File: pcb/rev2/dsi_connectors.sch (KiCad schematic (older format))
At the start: 6 parts, among them CN2 AX3E41264, CN3 CONN_02X15_ALT

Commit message: pcb wip
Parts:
- added B5, B6: PLATED_HOLE0.8_PAD1.3, c130h80, symbol PLATED_HOLE0.8_PAD1.3
- CN2: footprint (none) -> dsi_shield:IPHONE4_LCD_CONN
- CN3: footprint (none) -> dsi_shield:GB042-30S-E1000
- R1, R2, R49, R50: footprint RESC1608X55N -> Resistors SMD:RESC1608X55N
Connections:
- net labels added: +5V
- wire segments 79 -> 83
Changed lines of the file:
@@
 F 0 "CN2" H 6450 2865 50  0000 C CNN
 F 1 "AX3E41264" H 6450 2774 50  0000 C CNN
-F 2 "" H 6450 900 50  0001 C CNN
+F 2 "dsi_shield:IPHONE4_LCD_CONN" H 6450 900 50  0001 C CNN
 F 3 "" H 6450 900 50  0001 C CNN
 	1    6450 2050
@@
 F 0 "R1" H 7650 1853 50  0000 C CNN
 F 1 "R0603_10R_1%_0.1W_200PPM" H 7500 1340 60  0001 L CNN
-F 2 "RESC1608X55N" H 7500 530 60  0001 L CNN
+F 2 "Resistors SMD:RESC1608X55N" H 7500 530 60  0001 L CNN
 F 3 "\\cern.ch\\dfs\\Applications\\Altium\\Datasheets\\R0603_NIC_NRC.pdf" H 7500 1160 60  0001 L CNN
 F 4 "Value" H 7500 1550 60  0001 C CNN "Fieldname"
@@
 F 0 "R2" H 7650 2147 50  0000 C CNN
 F 1 "R0603_3K3_1%_0.1W_100PPM" H 7500 1740 60  0001 L CNN
-F 2 "RESC1608X55N" H 7500 930 60  0001 L CNN
+F 2 "Resistors SMD:RESC1608X55N" H 7500 930 60  0001 L CNN
 F 3 "\\cern.ch\\dfs\\Applications\\Altium\\Datasheets\\R0603_NIC_NRC.pdf" H 7500 1560 60  0001 L CNN
 F 4 "3k3" H 7650 2056 50  0000 C CNN "~"
@@
 F 0 "CN3" H 6450 5865 50  0000 C CNN
 F 1 "CONN_02X15_ALT" H 6450 5774 50  0000 C CNN
-F 2 "" H 6450 3800 50  0001 C CNN
+F 2 "dsi_shield:GB042-30S-E1000" H 6450 3800 50  0001 C CNN
 F 3 "" H 6450 3800 50  0001 C CNN
 	1    6450 4950
@@
 F 0 "R49" H 7300 4547 50  0000 C CNN
 F 1 "R0603_10R_1%_0.1W_200PPM" H 7150 4140 60  0001 L CNN
-F 2 "RESC1608X55N" H 7150 3330 60  0001 L CNN
+F 2 "Resistors SMD:RESC1608X55N" H 7150 3330 60  0001 L CNN
 F 3 "\\cern.ch\\dfs\\Applications\\Altium\\Datasheets\\R0603_NIC_NRC.pdf" H 7150 3960 60  0001 L CNN
 F 4 "10" H 7300 4456 50  0000 C CNN "~"
@@
 F 0 "R50" H 7300 4345 50  0000 C CNN
 F 1 "R0603_10R_1%_0.1W_200PPM" H 7150 4240 60  0001 L CNN
-F 2 "RESC1608X55N" H 7150 3430 60  0001 L CNN
+F 2 "Resistors SMD:RESC1608X55N" H 7150 3430 60  0001 L CNN
 F 3 "\\cern.ch\\dfs\\Applications\\Altium\\Datasheets\\R0603_NIC_NRC.pdf" H 7150 4060 60  0001 L CNN
 F 4 "10" H 7450 4350 50  0000 C CNN "~"
@@
 Wire Notes Line
 	3100 6800 700  6800
+$Comp
+L PLATED_HOLE0.8_PAD1.3 B5
+U 1 1 599E1A70
+P 2500 5000
+F 0 "B5" H 2485 5105 50  0000 C CNN
+F 1 "PLATED_HOLE0.8_PAD1.3" H 2500 4830 60  0001 L CNN
+F 2 "c130h80" H 2500 4020 60  0001 L CNN
+F 3 "Undefined" H 2500 4650 60  0001 L CNN
+F 4 "Plated Hole" H 2500 4560 60  0001 L CNN "Field4"
+F 5 "PLATED_HOLE0.8_PAD1.3" H 2500 4560 60  0001 L CNN "Part Number"
+F 6 "Single Terminal Socket" H 2500 4470 60  0001 L CNN "Library Ref"
+F 7 "SchLib\\Pads.SchLib" H 2500 4380 60  0001 L CNN "Library Path"
+F 8 "~~" H 2500 4290 60  0001 L CNN "Comment"
+F 9 "Standard (No BOM)" H 2500 4200 60  0001 L CNN "Component Kind"
+F 10 "Standard (No BOM)" H 2500 4110 60  0001 L CNN "Component Type"
+F 11 "1" H 2500 3930 60  0001 L CNN "Pin Count"
+F 12 "~~" H 2500 3840 60  0001 L CNN "Case"
+F 13 "PcbLib\\Pads.PcbLib" H 2500 3750 60  0001 L CNN "Footprint Path"
+F 14 "c130h80" H 2500 3660 60  0001 L CNN "Footprint Ref"
+F 15 "Plated Hole" H 2500 3570 60  0001 L CNN "Family"
+F 16 "No" H 2500 3480 60  0001 L CNN "Mounted"
+F 17 "No" H 2500 3390 60  0001 L CNN "Socket"
+F 18 "No" H 2500 3300 60  0001 L CNN "SMD"
+F 19 "No" H 2500 3210 60  0001 L CNN "Sense"
+F 20 "~~" H 2500 3120 60  0001 L CNN "Sense Comment"
+F 21 "None" H 2500 3030 60  0001 L CNN "Status"
+F 22 "~~" H 2500 2940 60  0001 L CNN "Status Comment"
+F 23 "~~" H 2500 2850 60  0001 L CNN "SCEM"
+F 24 "Plated Through Hole: Hole Dia.=0.8mm Pad Dia.=1.3mm, IPC-7251 Level C" H 2500 2760 60  0001 L CNN "Part Description"
+F 25 "~~" H 2500 2670 60  0001 L CNN "Manufacturer"
+F 26 "~~" H 2500 2580 60  0001 L CNN "Manufacturer Part Number"
+F 27 "0mm" H 2500 2490 60  0001 L CNN "ComponentHeight"
+F 28 "~~" H 2500 2400 60  0001 L CNN "Manufacturer1 Example"
+F 29 "~~" H 2500 2310 60  0001 L CNN "Manufacturer1 Part Number"
+F 30 "~~" H 2500 2220 60  0001 L CNN "Manufacturer1 ComponentHeight"
+F 31 "Undefined" H 2500 2130 60  0001 L CNN "HelpURL"
+F 32 "~~" H 2500 2040 60  0001 L CNN "ComponentLink1URL"
+F 33 "~~" H 2500 1950 60  0001 L CNN "ComponentLink1Description"
+F 34 "~~" H 2500 1860 60  0001 L CNN "ComponentLink2URL"
+F 35 "~~" H 2500 1770 60  0001 L CNN "ComponentLink2Description"
+F 36 "CERN DEM JLC" H 2500 1680 60  0001 L CNN "Author"
+F 37 "10/30/08 00:00:00" H 2500 1590 60  0001 L CNN "CreateDate"
+F 38 "10/30/08 00:00:00" H 2500 1500 60  0001 L CNN "LatestRevisionDate"
+F 39 "Plated Through Hole: Hole Dia.=0.8mm Pad Dia.=1.3mm, IPC-7251 Level C" H 2500 1410 60  0001 L CNN "PackageDescription"
+F 40 "Pads" H 2500 1320 60  0001 L CNN "Library Name"
+F 41 "This work is licensed under the Creative Commons CC-BY-SA 4.0 License. To the extent that circuit schematics that use Licensed Material can be considered to be ‘Adapted Material’, then the copyright holder waives article 3.b of the license with respect to these schematics." H 2500 1230 60  0001 L CNN "License"
+	1    2500 5000
+	1    0    0    -1
+$EndComp
+$Comp
+L PLATED_HOLE0.8_PAD1.3 B6
+U 1 1 599E1C02
+P 2500 5250
+F 0 "B6" H 2485 5355 50  0000 C CNN
+F 1 "PLATED_HOLE0.8_PAD1.3" H 2500 5080 60  0001 L CNN
+F 2 "c130h80" H 2500 4270 60  0001 L CNN
+F 3 "Undefined" H 2500 4900 60  0001 L CNN
+F 4 "Plated Hole" H 2500 4810 60  0001 L CNN "Field4"
+F 5 "PLATED_HOLE0.8_PAD1.3" H 2500 4810 60  0001 L CNN "Part Number"
+F 6 "Single Terminal Socket" H 2500 4720 60  0001 L CNN "Library Ref"
+F 7 "SchLib\\Pads.SchLib" H 2500 4630 60  0001 L CNN "Library Path"
+F 8 "~~" H 2500 4540 60  0001 L CNN "Comment"
+F 9 "Standard (No BOM)" H 2500 4450 60  0001 L CNN "Component Kind"
+F 10 "Standard (No BOM)" H 2500 4360 60  0001 L CNN "Component Type"
+F 11 "1" H 2500 4180 60  0001 L CNN "Pin Count"
+F 12 "~~" H 2500 4090 60  0001 L CNN "Case"
+F 13 "PcbLib\\Pads.PcbLib" H 2500 4000 60  0001 L CNN "Footprint Path"
+F 14 "c130h80" H 2500 3910 60  0001 L CNN "Footprint Ref"
+F 15 "Plated Hole" H 2500 3820 60  0001 L CNN "Family"
+F 16 "No" H 2500 3730 60  0001 L CNN "Mounted"
+F 17 "No" H 2500 3640 60  0001 L CNN "Socket"
+F 18 "No" H 2500 3550 60  0001 L CNN "SMD"
+F 19 "No" H 2500 3460 60  0001 L CNN "Sense"
+F 20 "~~" H 2500 3370 60  0001 L CNN "Sense Comment"
+F 21 "None" H 2500 3280 60  0001 L CNN "Status"
+F 22 "~~" H 2500 3190 60  0001 L CNN "Status Comment"
+F 23 "~~" H 2500 3100 60  0001 L CNN "SCEM"
+F 24 "Plated Through Hole: Hole Dia.=0.8mm Pad Dia.=1.3mm, IPC-7251 Level C" H 2500 3010 60  0001 L CNN "Part Description"
+F 25 "~~" H 2500 2920 60  0001 L CNN "Manufacturer"
+F 26 "~~" H 2500 2830 60  0001 L CNN "Manufacturer Part Number"
+F 27 "0mm" H 2500 2740 60  0001 L CNN "ComponentHeight"
+F 28 "~~" H 2500 2650 60  0001 L CNN "Manufacturer1 Example"
+F 29 "~~" H 2500 2560 60  0001 L CNN "Manufacturer1 Part Number"
+F 30 "~~" H 2500 2470 60  0001 L CNN "Manufacturer1 ComponentHeight"
+F 31 "Undefined" H 2500 2380 60  0001 L CNN "HelpURL"
+F 32 "~~" H 2500 2290 60  0001 L CNN "ComponentLink1URL"
+F 33 "~~" H 2500 2200 60  0001 L CNN "ComponentLink1Description"
+F 34 "~~" H 2500 2110 60  0001 L CNN "ComponentLink2URL"
+F 35 "~~" H 2500 2020 60  0001 L CNN "ComponentLink2Description"
+F 36 "CERN DEM JLC" H 2500 1930 60  0001 L CNN "Author"
+F 37 "10/30/08 00:00:00" H 2500 1840 60  0001 L CNN "CreateDate"
+F 38 "10/30/08 00:00:00" H 2500 1750 60  0001 L CNN "LatestRevisionDate"
+F 39 "Plated Through Hole: Hole Dia.=0.8mm Pad Dia.=1.3mm, IPC-7251 Level C" H 2500 1660 60  0001 L CNN "PackageDescription"
+F 40 "Pads" H 2500 1570 60  0001 L CNN "Library Name"
+F 41 "This work is licensed under the Creative Commons CC-BY-SA 4.0 License. To the extent that circuit schematics that use Licensed Material can be considered to be ‘Adapted Material’, then the copyright holder waives article 3.b of the license with respect to these schematics." H 2500 1480 60  0001 L CNN "License"
+	1    2500 5250
+	1    0    0    -1
+$EndComp
+$Comp
+L GND #PWR?
+U 1 1 599E1E7E
+P 2850 5350
+F 0 "#PWR?" H 2850 5100 50  0001 C CNN
+F 1 "GND" H 2855 5177 50  0000 C CNN
+F 2 "" H 2850 5350 50  0001 C CNN
+F 3 "" H 2850 5350 50  0001 C CNN
+	1    2850 5350
+	1    0    0    -1
+$EndComp
+Wire Wire Line
+	2500 5250 2850 5250
+Wire Wire Line
+	2850 5250 2850 5350
+$Comp
+L +5V #PWR?
+U 1 1 599E219E
+P 2850 4850
+F 0 "#PWR?" H 2850 4700 50  0001 C CNN
+F 1 "+5V" H 2865 5023 50  0000 C CNN
+F 2 "" H 2850 4850 50  0001 C CNN
+F 3 "" H 2850 4850 50  0001 C CNN
+	1    2850 4850
+	1    0    0    -1
+$EndComp
+Wire Wire Line
+	2500 5000 2850 5000
+Wire Wire Line
+	2850 5000 2850 4850
 $EndSCHEMATC

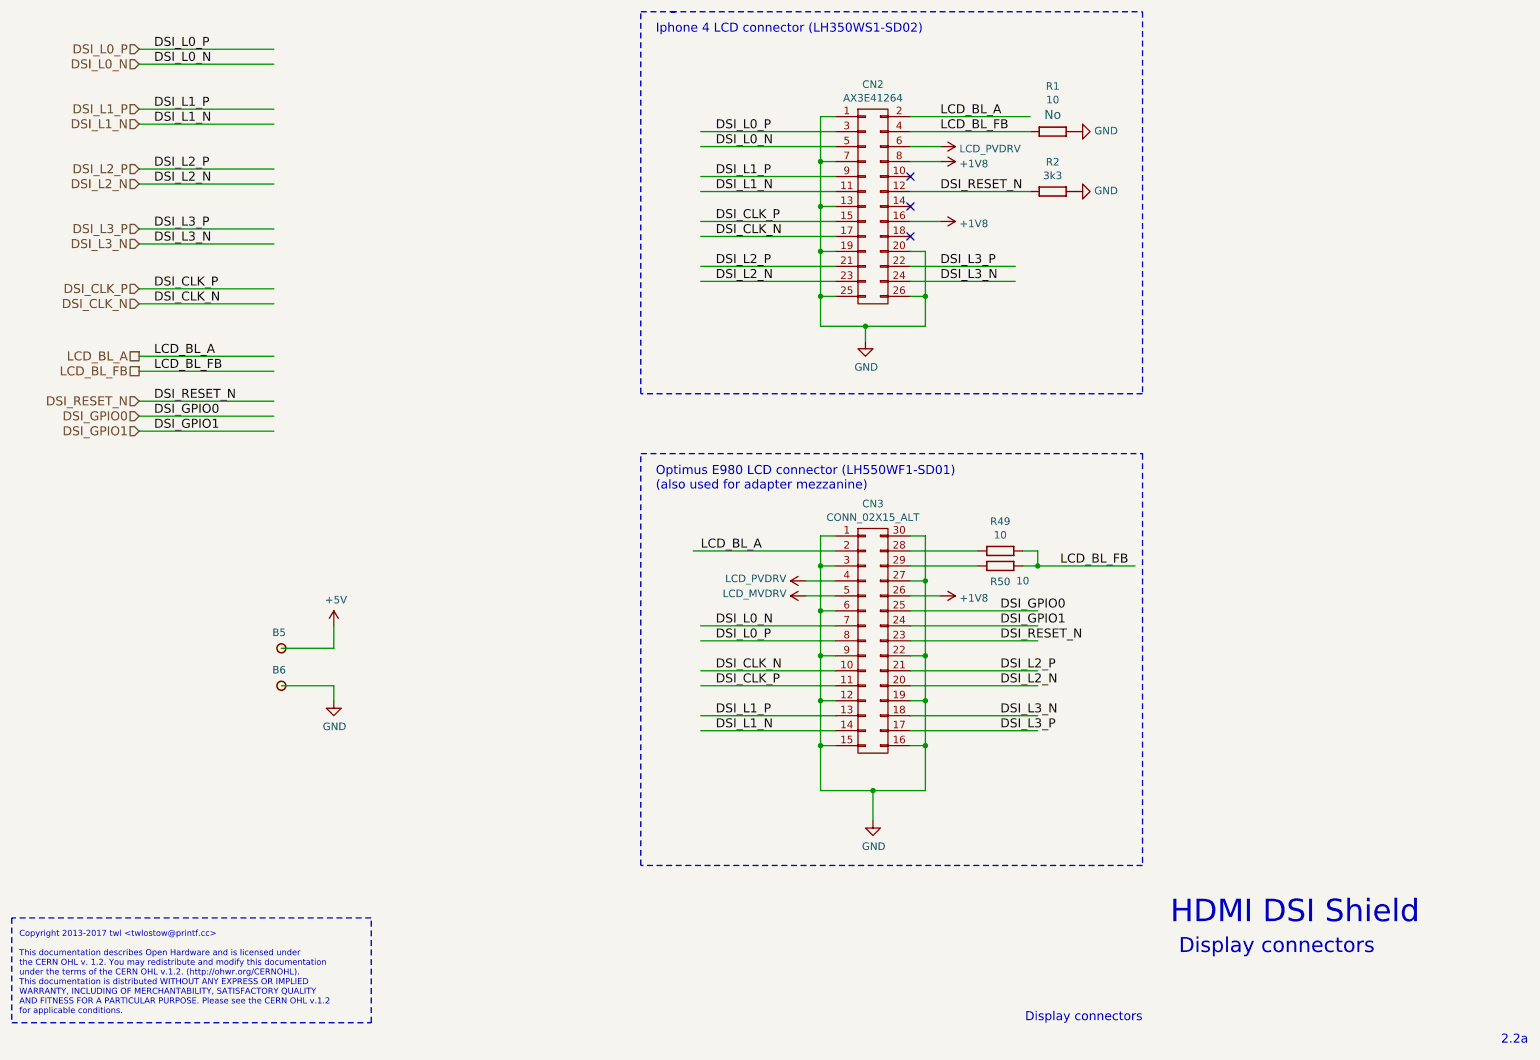
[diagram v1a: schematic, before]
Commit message: Completed port to KiCad, passes DRC+LVS. NOT MANUFACTURED.
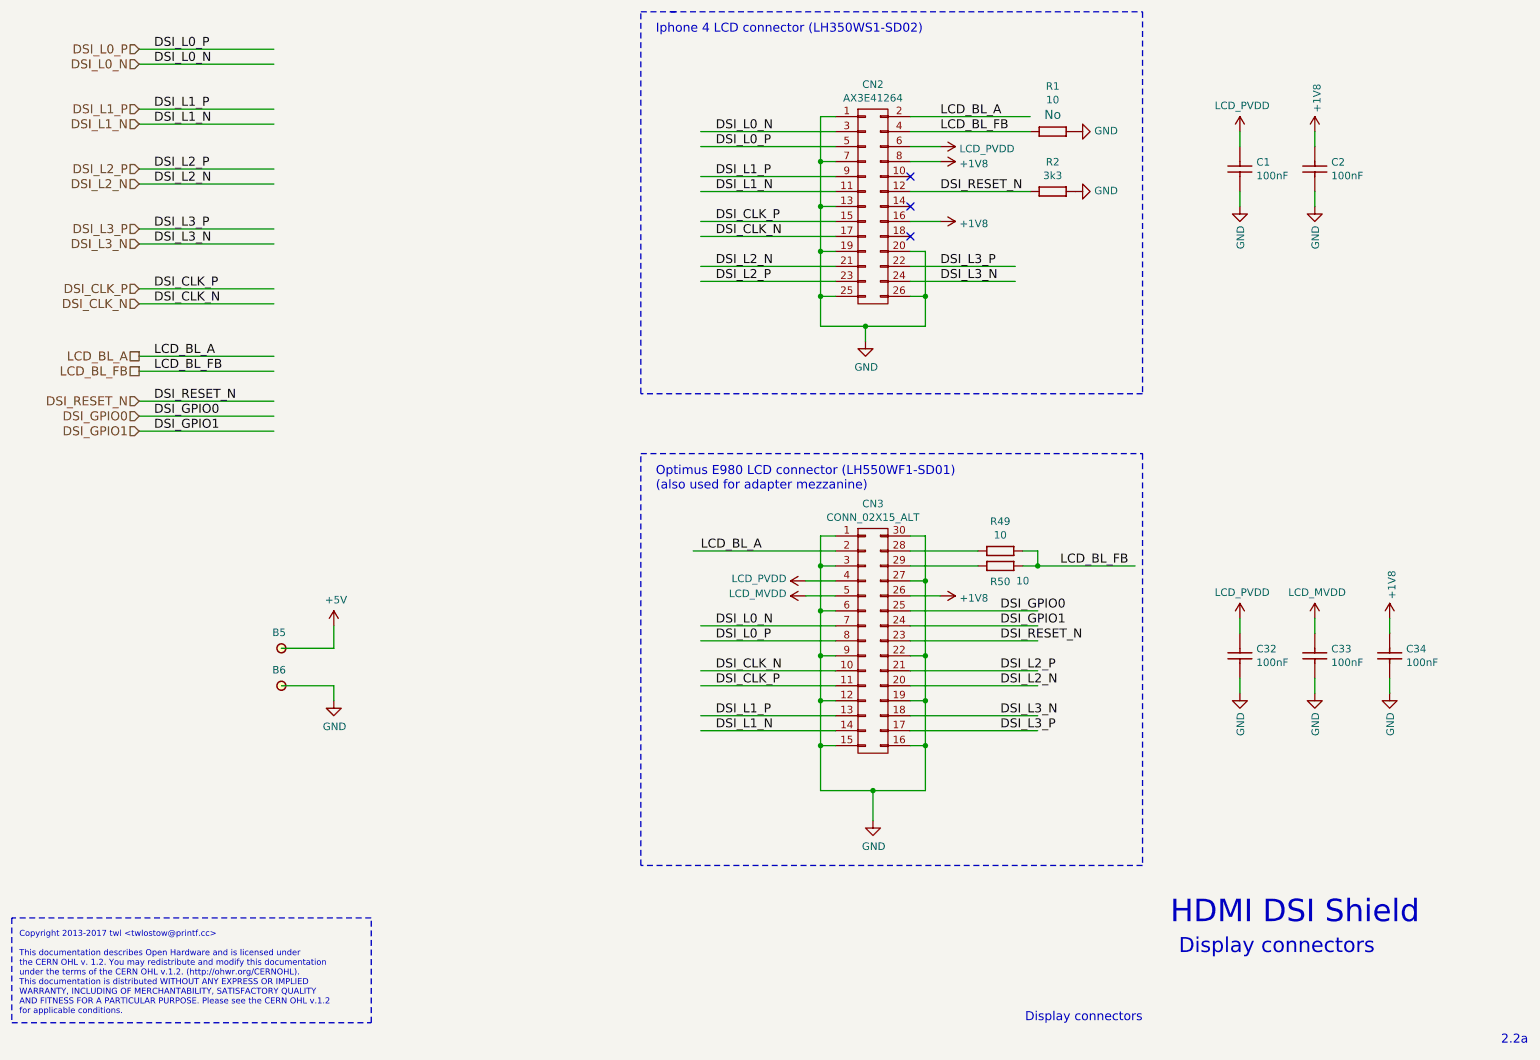
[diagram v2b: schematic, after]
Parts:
- added C1, C2, C32, C33, C34: CC0603_100NF_100V_10%_X7R, CAPC1608X90N, symbol CC0603_100NF_100V_10%_X7R
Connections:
- net labels added: LCD_MVDD, LCD_PVDD
- net labels removed: LCD_MVDRV, LCD_PVDRV
- wire segments 83 -> 93

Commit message: axi4/zynq version: wip
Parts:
- B5, B6: symbol PLATED_HOLE0.8_PAD1.3 -> dsi_shield-rescue:PLATED_HOLE0.8_PAD1.3-
- C1, C2, C32, C33, C34: symbol CC0603_100NF_100V_10%_X7R -> dsi_shield-rescue:CC0603_100NF_100V_10%_X7R-
- CN2: symbol CONN_02X13 -> dsi_shield-rescue:CONN_02X13-
- CN3: symbol CONN_02X15_ALT -> dsi_shield-rescue:CONN_02X15_ALT-
- R1, R49, R50: symbol R0603_10R_1%_0.1W_200PPM -> dsi_shield-rescue:R0603_10R_1%_0.1W_200PPM-
- R2: symbol R0603_3K3_1%_0.1W_100PPM -> dsi_shield-rescue:R0603_3K3_1%_0.1W_100PPM-
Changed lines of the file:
@@
-EESchema Schematic File Version 2
-LIBS:Capacitors Networks THD
-LIBS:Capacitors Networks SMD
-LIBS:Capacitors THD
-LIBS:Capacitors SMD
-LIBS:Miscellaneous
-LIBS:HARWIN
-LIBS:LEMO
-LIBS:WEIDMULLER
-LIBS:FCI
-LIBS:MOLEX
-LIBS:TYCO
-LIBS:ERNI
-LIBS:MENTOR
-LIBS:SAMTEC
-LIBS:STELVIO-KONTEK COMATEL
-LIBS:AMPHENOL
-LIBS:HARTING
-LIBS:3M
-LIBS:Pads
-LIBS:Switches
-LIBS:Relays
-LIBS:Heat-Sinks
-LIBS:Fasteners & Fixings
-LIBS:Batteries
-LIBS:Fuses
-LIBS:Metal Screening Box
-LIBS:Sockets
-LIBS:Regulators
-LIBS:Transistors
-LIBS:Power Supplies
-LIBS:Analog & Interface
-LIBS:Sensors
-LIBS:Logic
-LIBS:Optocouplers
-LIBS:Standard Logic
-LIBS:DC-DC Converters
-LIBS:Operational Amplifiers
-LIBS:Crystals & Oscillators
-LIBS:Diodes
-LIBS:LEDs & Displays
-LIBS:PCB Modules
-LIBS:Bonding
-LIBS:Resistors THD
-LIBS:Potentiometers SMD
-LIBS:Thermistors And Varistors
-LIBS:Potentiometers THD
-LIBS:Resistor Networks THD
-LIBS:Resistors SMD
-LIBS:Resistor Networks SMD
-LIBS:Transformers
-LIBS:Inductors SMD
-LIBS:Inductors THD
-LIBS:Cores
-LIBS:power
-LIBS:conn
-LIBS:dsi_shield
+EESchema Schematic File Version 4
 LIBS:dsi_shield-cache
 EELAYER 26 0
@@
 $EndDescr
 $Comp
-L CONN_02X13 CN2
+L dsi_shield-rescue:CONN_02X13- CN2
 U 1 1 5992BEF4
 P 6450 2050
@@
 LCD_BL_FB
 $Comp
-L R0603_10R_1%_0.1W_200PPM R1
+L dsi_shield-rescue:R0603_10R_1%_0.1W_200PPM- R1
 U 1 1 5992DD51
 P 7500 1550
@@
 $EndComp
 $Comp
-L +1V8 #PWR0133
+L dsi_shield-rescue:+1V8- #PWR0133
 U 1 1 5992E6B7
 P 6900 1750
@@
 NoConn ~ 6700 2050
 $Comp
-L +1V8 #PWR0134
+L dsi_shield-rescue:+1V8- #PWR0134
 U 1 1 5992E849
 P 6900 2150
@@
 	6700 2150 6900 2150
 $Comp
-L R0603_3K3_1%_0.1W_100PPM R2
+L dsi_shield-rescue:R0603_3K3_1%_0.1W_100PPM- R2
 U 1 1 599346A2
 P 7500 1950
@@
 Connection ~ 6400 2850
 $Comp
-L GND #PWR0135
+L dsi_shield-rescue:GND- #PWR0135
 U 1 1 5993C371
 P 6400 2950
@@
 $EndComp
 $Comp
-L GND #PWR0136
+L dsi_shield-rescue:GND- #PWR0136
 U 1 1 5993C3F9
 P 7800 1550
@@
 $EndComp
 $Comp
-L GND #PWR0137
+L dsi_shield-rescue:GND- #PWR0137
 U 1 1 5993C774
 P 7800 1950
@@
 	1550 3550 2450 3550
 $Comp
-L CONN_02X15_ALT CN3
+L dsi_shield-rescue:CONN_02X15_ALT- CN3
 U 1 1 59949FB3
 P 6450 4950
@@
 	6700 4350 7150 4350
 $Comp
-L R0603_10R_1%_0.1W_200PPM R49
+L dsi_shield-rescue:R0603_10R_1%_0.1W_200PPM- R49
 U 1 1 5994AFFA
 P 7150 4350
@@
 $EndComp
 $Comp
-L R0603_10R_1%_0.1W_200PPM R50
+L dsi_shield-rescue:R0603_10R_1%_0.1W_200PPM- R50
 U 1 1 5994B12D
 P 7150 4450
@@
 	6700 4650 6900 4650
 $Comp
-L +1V8 #PWR0138
+L dsi_shield-rescue:+1V8- #PWR0138
 U 1 1 5994CF83
 P 6900 4650
@@
 	6200 4650 6000 4650
 $Comp
-L GND #PWR0141
+L dsi_shield-rescue:GND- #PWR0141
 U 1 1 59956F93
 P 6450 6150
@@
 	3100 6800 700  6800
 $Comp
-L PLATED_HOLE0.8_PAD1.3 B5
+L dsi_shield-rescue:PLATED_HOLE0.8_PAD1.3- B5
 U 1 1 599E1A70
 P 2500 5000
@@
 $EndComp
 $Comp
-L PLATED_HOLE0.8_PAD1.3 B6
+L dsi_shield-rescue:PLATED_HOLE0.8_PAD1.3- B6
 U 1 1 599E1C02
 P 2500 5250
@@
 $EndComp
 $Comp
-L GND #PWR0132
+L dsi_shield-rescue:GND- #PWR0132
 U 1 1 599E1E7E
 P 2850 5350
@@
 	2850 5250 2850 5350
 $Comp
-L +5V #PWR0139
+L dsi_shield-rescue:+5V- #PWR0139
 U 1 1 599E219E
 P 2850 4850
@@
 	2850 5000 2850 4850
 $Comp
-L LCD_PVDD #PWR0140
+L dsi_shield-rescue:LCD_PVDD- #PWR0140
 U 1 1 599DFBF6
 P 6900 1650
@@
 $EndComp
 $Comp
-L LCD_PVDD #PWR0142
+L dsi_shield-rescue:LCD_PVDD- #PWR0142
 U 1 1 599E01CB
 P 6000 4550
@@
 $EndComp
 $Comp
-L LCD_MVDD #PWR0143
+L dsi_shield-rescue:LCD_MVDD- #PWR0143
 U 1 1 599E04B6
 P 6000 4650
@@
 $EndComp
 $Comp
-L LCD_PVDD #PWR0144
+L dsi_shield-rescue:LCD_PVDD- #PWR0144
 U 1 1 599E0758
 P 8900 1550
@@
 $EndComp
 $Comp
-L +1V8 #PWR0145
+L dsi_shield-rescue:+1V8- #PWR0145
 U 1 1 599E078B
 P 9400 1550
@@
 $EndComp
 $Comp
-L CC0603_100NF_100V_10%_X7R C1
+L dsi_shield-rescue:CC0603_100NF_100V_10%_X7R- C1
 U 1 1 599E1407
 P 8900 1650
@@
 $EndComp
 $Comp
-L CC0603_100NF_100V_10%_X7R C2
+L dsi_shield-rescue:CC0603_100NF_100V_10%_X7R- C2
 U 1 1 599E1572
 P 9400 1650
@@
 	8900 1550 8900 1650
 $Comp
-L GND #PWR0146
+L dsi_shield-rescue:GND- #PWR0146
 U 1 1 599E1772
 P 9400 2050
@@
 	9400 1950 9400 2050
 $Comp
-L GND #PWR0147
+L dsi_shield-rescue:GND- #PWR0147
 U 1 1 599E188B
 P 8900 2050
@@
 	8900 1950 8900 2050
 $Comp
-L LCD_PVDD #PWR0148
+L dsi_shield-rescue:LCD_PVDD- #PWR0148
 U 1 1 599E3395
 P 8900 4800
@@
 $EndComp
 $Comp
-L +1V8 #PWR0149
+L dsi_shield-rescue:+1V8- #PWR0149
 U 1 1 599E339B
 P 9900 4800
@@
 $EndComp
 $Comp
-L CC0603_100NF_100V_10%_X7R C32
+L dsi_shield-rescue:CC0603_100NF_100V_10%_X7R- C32
 U 1 1 599E33C6
 P 8900 4900
@@
 $EndComp
 $Comp
-L CC0603_100NF_100V_10%_X7R C34
+L dsi_shield-rescue:CC0603_100NF_100V_10%_X7R- C34
 U 1 1 599E33F2
 P 9900 4900
@@
 	8900 4800 8900 4900
 $Comp
-L GND #PWR0150
+L dsi_shield-rescue:GND- #PWR0150
 U 1 1 599E33FB
 P 9900 5300
@@
 	9900 5200 9900 5300
 $Comp
-L GND #PWR0151
+L dsi_shield-rescue:GND- #PWR0151
 U 1 1 599E3402
 P 8900 5300
@@
 	8900 5200 8900 5300
 $Comp
-L CC0603_100NF_100V_10%_X7R C33
+L dsi_shield-rescue:CC0603_100NF_100V_10%_X7R- C33
 U 1 1 599E34F6
 P 9400 4900
@@
 	9400 4800 9400 4900
 $Comp
-L GND #PWR0152
+L dsi_shield-rescue:GND- #PWR0152
 U 1 1 599E34FE
 P 9400 5300
@@
 	9400 5200 9400 5300
 $Comp
-L LCD_MVDD #PWR0153
+L dsi_shield-rescue:LCD_MVDD- #PWR0153
 U 1 1 599E3520
 P 9400 4800
